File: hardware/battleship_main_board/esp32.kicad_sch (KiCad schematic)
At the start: 0 parts

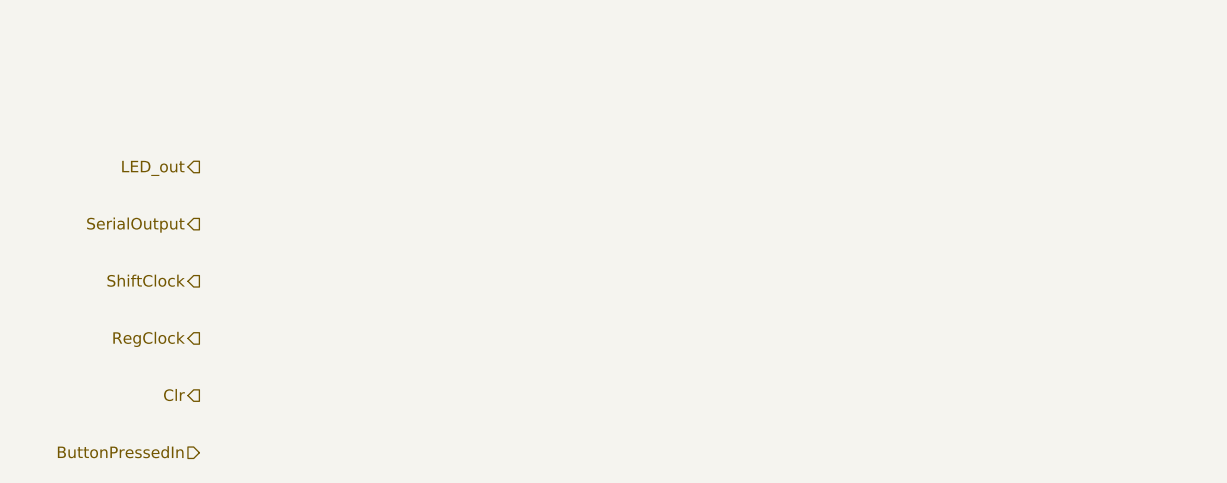
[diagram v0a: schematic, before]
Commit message: Got schematic to place that can be turned into a ratsnest
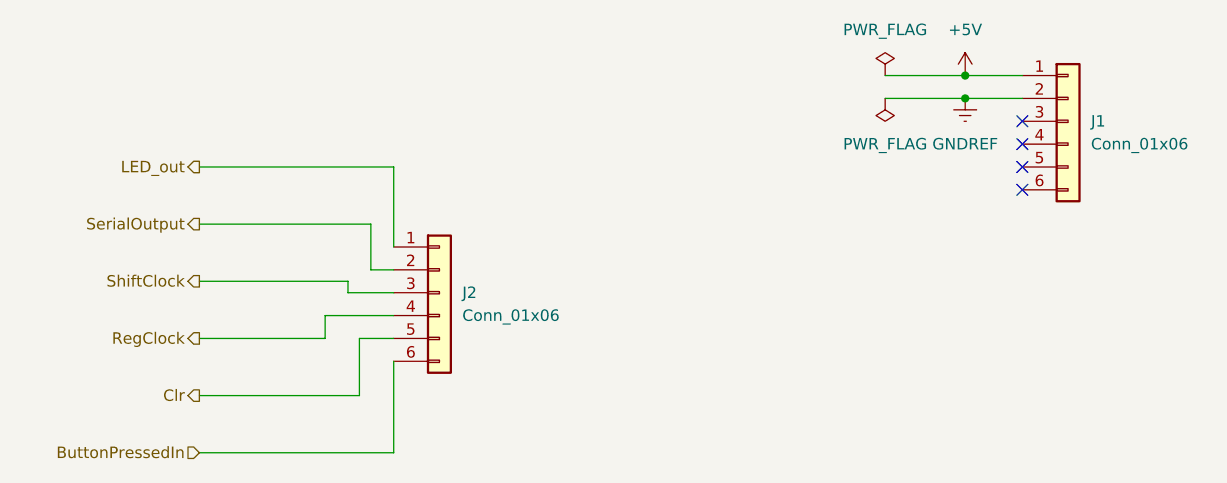
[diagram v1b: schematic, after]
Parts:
- added J1, J2: Conn_01x06, Connector_PinHeader_2.54mm:PinHeader_1x06_P2.54mm_Vertical, symbol Connector_Generic:Conn_01x06
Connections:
- net ButtonPressedIn: now also J2.6 (Pin_6)
- net Clr: now also J2.5 (Pin_5)
- net LED_out: now also J2.1 (Pin_1)
- net RegClock: now also J2.4 (Pin_4)
- net SerialOutput: now also J2.2 (Pin_2)
- net ShiftClock: now also J2.3 (Pin_3)
- new net +5V: J1.1 (Pin_1)
- new net GNDREF: J1.2 (Pin_2)
- no-connect marks 0 -> 4
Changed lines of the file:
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@@
 (kicad_sch (version 20211123) (generator eeschema)
   (paper "A4")
+  (junction (at 199.39 53.34) (diameter 0) (color 0 0 0 0)
+  )
+  (junction (at 199.39 50.8) (diameter 0) (color 0 0 0 0)
+  )
+  (no_connect (at 205.74 63.5))
+  (no_connect (at 205.74 58.42))
+  (no_connect (at 205.74 60.96))
+  (no_connect (at 205.74 55.88))
+  (wire (pts (xy 130.81 73.66) (xy 130.81 74.93))
+    (stroke (width 0) (type default) (color 0 0 0 0))
+  )
+  (wire (pts (xy 132.08 86.36) (xy 132.08 80.01))
+    (stroke (width 0) (type default) (color 0 0 0 0))
+  )
+  (wire (pts (xy 132.08 80.01) (xy 135.89 80.01))
+    (stroke (width 0) (type default) (color 0 0 0 0))
+  )
+  (wire (pts (xy 114.3 67.31) (xy 133.35 67.31))
+    (stroke (width 0) (type default) (color 0 0 0 0))
+  )
+  (wire (pts (xy 135.89 92.71) (xy 135.89 82.55))
+    (stroke (width 0) (type default) (color 0 0 0 0))
+  )
+  (wire (pts (xy 114.3 80.01) (xy 128.27 80.01))
+    (stroke (width 0) (type default) (color 0 0 0 0))
+  )
+  (wire (pts (xy 133.35 67.31) (xy 133.35 72.39))
+    (stroke (width 0) (type default) (color 0 0 0 0))
+  )
+  (wire (pts (xy 114.3 86.36) (xy 132.08 86.36))
+    (stroke (width 0) (type default) (color 0 0 0 0))
+  )
+  (wire (pts (xy 114.3 60.96) (xy 135.89 60.96))
+    (stroke (width 0) (type default) (color 0 0 0 0))
+  )
+  (wire (pts (xy 199.39 50.8) (xy 205.74 50.8))
+    (stroke (width 0) (type default) (color 0 0 0 0))
+  )
+  (wire (pts (xy 114.3 92.71) (xy 135.89 92.71))
+    (stroke (width 0) (type default) (color 0 0 0 0))
+  )
+  (wire (pts (xy 190.5 50.8) (xy 199.39 50.8))
+    (stroke (width 0) (type default) (color 0 0 0 0))
+  )
+  (wire (pts (xy 128.27 80.01) (xy 128.27 77.47))
+    (stroke (width 0) (type default) (color 0 0 0 0))
+  )
+  (wire (pts (xy 199.39 53.34) (xy 205.74 53.34))
+    (stroke (width 0) (type default) (color 0 0 0 0))
+  )
+  (wire (pts (xy 114.3 73.66) (xy 130.81 73.66))
+    (stroke (width 0) (type default) (color 0 0 0 0))
+  )
+  (wire (pts (xy 130.81 74.93) (xy 135.89 74.93))
+    (stroke (width 0) (type default) (color 0 0 0 0))
+  )
+  (wire (pts (xy 135.89 60.96) (xy 135.89 69.85))
+    (stroke (width 0) (type default) (color 0 0 0 0))
+  )
+  (wire (pts (xy 133.35 72.39) (xy 135.89 72.39))
+    (stroke (width 0) (type default) (color 0 0 0 0))
+  )
+  (wire (pts (xy 128.27 77.47) (xy 135.89 77.47))
+    (stroke (width 0) (type default) (color 0 0 0 0))
+  )
+  (wire (pts (xy 190.5 53.34) (xy 199.39 53.34))
+    (stroke (width 0) (type default) (color 0 0 0 0))
+  )
   (hierarchical_label "ShiftClock" (shape output) (at 114.3 73.66 180)
     (effects (font (size 1.27 1.27)) (justify right))
@@
     (effects (font (size 1.27 1.27)) (justify right))
   )
+  (symbol (lib_id "Connector_Generic:Conn_01x06") (at 210.82 55.88 0) (unit 1)
+    (in_bom yes) (on_board yes) (fields_autoplaced)
+    (property "Reference" "J1" (id 0) (at 213.36 55.8799 0)
+      (effects (font (size 1.27 1.27)) (justify left))
+    )
+    (property "Value" "Conn_01x06" (id 1) (at 213.36 58.4199 0)
+      (effects (font (size 1.27 1.27)) (justify left))
+    )
+    (property "Footprint" "Connector_PinHeader_2.54mm:PinHeader_1x06_P2.54mm_Vertical" (id 2) (at 210.82 55.88 0)
+      (effects (font (size 1.27 1.27)) hide)
+    )
+    (property "Datasheet" "~" (id 3) (at 210.82 55.88 0)
+      (effects (font (size 1.27 1.27)) hide)
+    )
+    (pin "1")
+    (pin "2")
+    (pin "3")
+    (pin "4")
+    (pin "5")
+    (pin "6")
+  )
+  (symbol (lib_id "Connector_Generic:Conn_01x06") (at 140.97 74.93 0) (unit 1)
+    (in_bom yes) (on_board yes) (fields_autoplaced)
+    (property "Reference" "J2" (id 0) (at 143.51 74.9299 0)
+      (effects (font (size 1.27 1.27)) (justify left))
+    )
+    (property "Value" "Conn_01x06" (id 1) (at 143.51 77.4699 0)
+      (effects (font (size 1.27 1.27)) (justify left))
+    )
+    (property "Footprint" "Connector_PinHeader_2.54mm:PinHeader_1x06_P2.54mm_Vertical" (id 2) (at 140.97 74.93 0)
+      (effects (font (size 1.27 1.27)) hide)
+    )
+    (property "Datasheet" "~" (id 3) (at 140.97 74.93 0)
+      (effects (font (size 1.27 1.27)) hide)
+    )
+    (pin "1")
+    (pin "2")
+    (pin "3")
+    (pin "4")
+    (pin "5")
+    (pin "6")
+  )
+  (symbol (lib_id "power:PWR_FLAG") (at 190.5 53.34 180) (unit 1)
+    (in_bom yes) (on_board yes) (fields_autoplaced)
+    (property "Reference" "#FLG02" (id 0) (at 190.5 55.245 0)
+      (effects (font (size 1.27 1.27)) hide)
+    )
+    (property "Value" "PWR_FLAG" (id 1) (at 190.5 58.42 0))
+    (property "Footprint" "" (id 2) (at 190.5 53.34 0)
+      (effects (font (size 1.27 1.27)) hide)
+    )
+    (property "Datasheet" "~" (id 3) (at 190.5 53.34 0)
+      (effects (font (size 1.27 1.27)) hide)
+    )
+    (pin "1")
+  )
+  (symbol (lib_id "power:GNDREF") (at 199.39 53.34 0) (unit 1)
+    (in_bom yes) (on_board yes) (fields_autoplaced)
+    (property "Reference" "#PWR049" (id 0) (at 199.39 59.69 0)
+      (effects (font (size 1.27 1.27)) hide)
+    )
+    (property "Value" "GNDREF" (id 1) (at 199.39 58.42 0))
+    (property "Footprint" "" (id 2) (at 199.39 53.34 0)
+      (effects (font (size 1.27 1.27)) hide)
+    )
+    (property "Datasheet" "" (id 3) (at 199.39 53.34 0)
+      (effects (font (size 1.27 1.27)) hide)
+    )
+    (pin "1")
+  )
+  (symbol (lib_id "power:+5V") (at 199.39 50.8 0) (unit 1)
+    (in_bom yes) (on_board yes) (fields_autoplaced)
+    (property "Reference" "#PWR048" (id 0) (at 199.39 54.61 0)
+      (effects (font (size 1.27 1.27)) hide)
+    )
+    (property "Value" "+5V" (id 1) (at 199.39 45.72 0))
+    (property "Footprint" "" (id 2) (at 199.39 50.8 0)
+      (effects (font (size 1.27 1.27)) hide)
+    )
+    (property "Datasheet" "" (id 3) (at 199.39 50.8 0)
+      (effects (font (size 1.27 1.27)) hide)
+    )
+    (pin "1")
+  )
+  (symbol (lib_id "power:PWR_FLAG") (at 190.5 50.8 0) (unit 1)
+    (in_bom yes) (on_board yes) (fields_autoplaced)
+    (property "Reference" "#FLG01" (id 0) (at 190.5 48.895 0)
+      (effects (font (size 1.27 1.27)) hide)
+    )
+    (property "Value" "PWR_FLAG" (id 1) (at 190.5 45.72 0))
+    (property "Footprint" "" (id 2) (at 190.5 50.8 0)
+      (effects (font (size 1.27 1.27)) hide)
+    )
+    (property "Datasheet" "~" (id 3) (at 190.5 50.8 0)
+      (effects (font (size 1.27 1.27)) hide)
+    )
+    (pin "1")
+  )
 )
